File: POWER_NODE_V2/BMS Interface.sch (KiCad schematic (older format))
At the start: 11 parts, among them J10 CONN_02X07, J9 CONN_01X02, U12 NCV8405ADTRKG, U13 MAX14850AEE+, U14 MAX14850AEE+

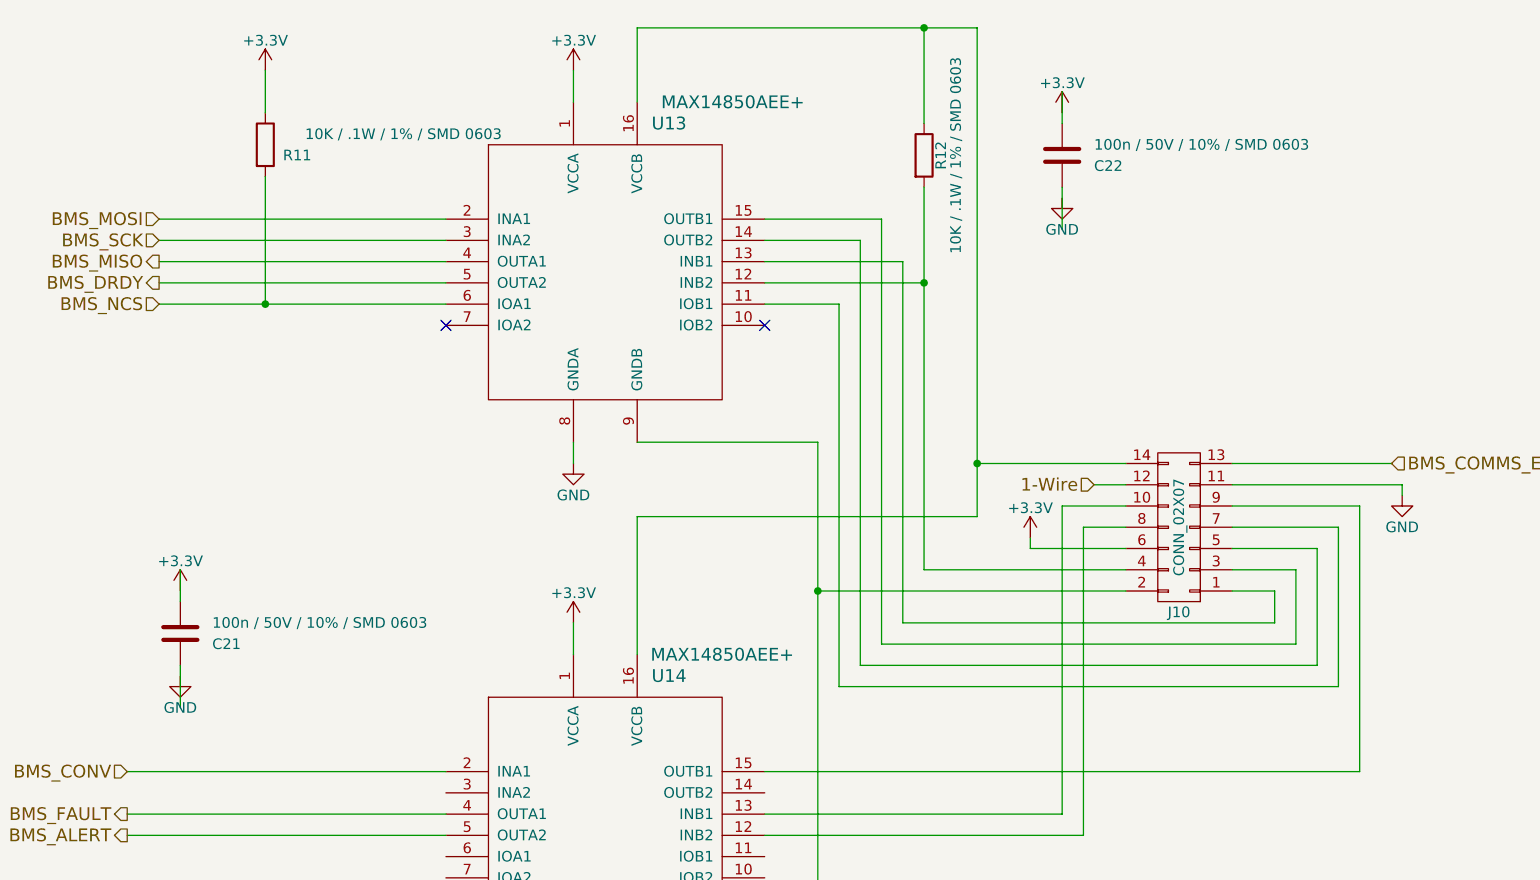
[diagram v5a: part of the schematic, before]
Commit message: Power Node v2 WIP
TODO: 3d models, double check everything, update connector P/N on
schematics, align boards and drill holes
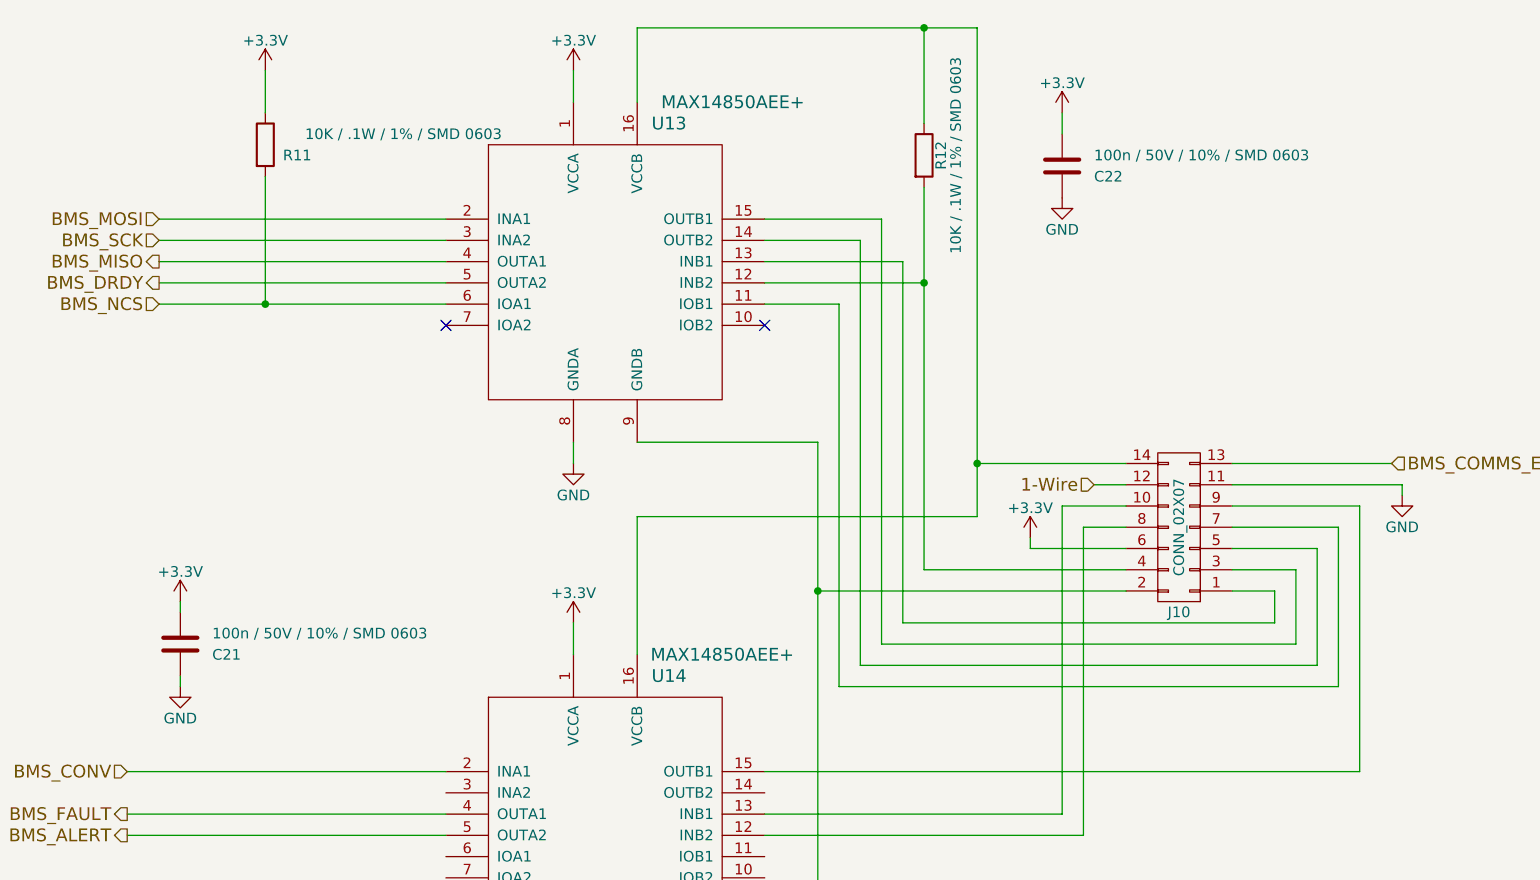
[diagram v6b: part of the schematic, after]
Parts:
- J9: footprint Pin_Headers:Pin_Header_Straight_1x02_Pitch2.54mm -> rLoop Footprints:TE_1744055-2_3.96_EP_HDR_ASSY_2P_VERT_HT
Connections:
- wire segments 78 -> 77
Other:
- moved on the sheet: C21, C22
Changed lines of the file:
@@
 F 0 "J9" H 5150 6700 50  0000 C CNN
 F 1 "CONN_01X02" V 5250 6550 50  0000 C CNN
-F 2 "Pin_Headers:Pin_Header_Straight_1x02_Pitch2.54mm" H 5150 6550 50  0001 C CNN
+F 2 "rLoop Footprints:TE_1744055-2_3.96_EP_HDR_ASSY_2P_VERT_HT" H 5150 6550 50  0001 C CNN
 F 3 "" H 5150 6550 50  0001 C CNN
 	1    5150 6550
@@
 L C C22
 U 1 1 59514BAA
-P 6450 1750
-F 0 "C22" H 6600 1700 50  0000 L CNN
-F 1 "100n / 50V / 10% / SMD 0603" H 6600 1800 50  0000 L CNN
-F 2 "Capacitors_SMD:C_0603" H 6488 1600 50  0001 C CNN
-F 3 "" H 6450 1750 50  0001 C CNN
-	1    6450 1750
+P 6450 1800
+F 0 "C22" H 6600 1750 50  0000 L CNN
+F 1 "100n / 50V / 10% / SMD 0603" H 6600 1850 50  0000 L CNN
+F 2 "Capacitors_SMD:C_0603" H 6488 1650 50  0001 C CNN
+F 3 "" H 6450 1800 50  0001 C CNN
+	1    6450 1800
 	1    0    0    -1
 $EndComp
@@
 $EndComp
 $Comp
-L GND #PWR0107
-U 1 1 59514D0B
-P 6450 1950
-F 0 "#PWR0107" H 6450 1700 50  0001 C CNN
-F 1 "GND" H 6450 1800 50  0000 C CNN
-F 2 "" H 6450 1950 50  0001 C CNN
-F 3 "" H 6450 1950 50  0001 C CNN
-	1    6450 1950
-	1    0    0    -1
-$EndComp
-$Comp
 L C C21
 U 1 1 59515426
-P 2300 4000
-F 0 "C21" H 2450 3950 50  0000 L CNN
-F 1 "100n / 50V / 10% / SMD 0603" H 2450 4050 50  0000 L CNN
-F 2 "Capacitors_SMD:C_0603" H 2338 3850 50  0001 C CNN
-F 3 "" H 2300 4000 50  0001 C CNN
-	1    2300 4000
-	1    0    0    -1
-$EndComp
-$Comp
-L +3.3V #PWR0108
+P 2300 4050
+F 0 "C21" H 2450 4000 50  0000 L CNN
+F 1 "100n / 50V / 10% / SMD 0603" H 2450 4100 50  0000 L CNN
+F 2 "Capacitors_SMD:C_0603" H 2338 3900 50  0001 C CNN
+F 3 "" H 2300 4050 50  0001 C CNN
+	1    2300 4050
+	1    0    0    -1
+$EndComp
+$Comp
+L +3.3V #PWR0107
 U 1 1 5951542C
-P 2300 3800
-F 0 "#PWR0108" H 2300 3650 50  0001 C CNN
-F 1 "+3.3V" H 2300 3940 50  0000 C CNN
-F 2 "" H 2300 3800 50  0001 C CNN
-F 3 "" H 2300 3800 50  0001 C CNN
-	1    2300 3800
-	1    0    0    -1
-$EndComp
-$Comp
-L GND #PWR0109
+P 2300 3850
+F 0 "#PWR0107" H 2300 3700 50  0001 C CNN
+F 1 "+3.3V" H 2300 3990 50  0000 C CNN
+F 2 "" H 2300 3850 50  0001 C CNN
+F 3 "" H 2300 3850 50  0001 C CNN
+	1    2300 3850
+	1    0    0    -1
+$EndComp
+$Comp
+L GND #PWR0108
 U 1 1 59515432
-P 2300 4200
-F 0 "#PWR0109" H 2300 3950 50  0001 C CNN
-F 1 "GND" H 2300 4050 50  0000 C CNN
-F 2 "" H 2300 4200 50  0001 C CNN
-F 3 "" H 2300 4200 50  0001 C CNN
-	1    2300 4200
+P 2300 4250
+F 0 "#PWR0108" H 2300 4000 50  0001 C CNN
+F 1 "GND" H 2300 4100 50  0000 C CNN
+F 2 "" H 2300 4250 50  0001 C CNN
+F 3 "" H 2300 4250 50  0001 C CNN
+	1    2300 4250
 	1    0    0    -1
 $EndComp
@@
 	0    1    1    0
 $EndComp
-Wire Wire Line
-	2200 2050 3550 2050
-Wire Wire Line
-	3550 2150 2200 2150
-Wire Wire Line
-	2200 2250 3550 2250
-Wire Wire Line
-	2200 2350 3550 2350
-Wire Wire Line
-	2050 4650 3550 4650
-Wire Wire Line
-	3550 4850 2050 4850
-Wire Wire Line
-	2050 4950 3550 4950
-Wire Wire Line
-	2200 2450 3550 2450
-Wire Wire Line
-	7250 3200 8000 3200
-Wire Wire Line
-	7250 3300 8050 3300
-Wire Wire Line
-	8050 3300 8050 3350
-Wire Wire Line
-	7250 3400 7850 3400
-Wire Wire Line
-	7850 3400 7850 4650
-Wire Wire Line
-	7850 4650 5050 4650
-Wire Wire Line
-	7250 3500 7750 3500
-Wire Wire Line
-	7750 3500 7750 4250
-Wire Wire Line
-	7750 4250 5400 4250
-Wire Wire Line
-	5400 4250 5400 2450
-Wire Wire Line
-	7250 3600 7650 3600
-Wire Wire Line
-	7650 3600 7650 4150
-Wire Wire Line
-	7650 4150 5500 4150
-Wire Wire Line
-	5500 4150 5500 2150
-Wire Wire Line
-	5500 2150 5050 2150
-Wire Wire Line
-	5400 2450 5050 2450
-Wire Wire Line
-	7250 3700 7550 3700
-Wire Wire Line
-	7550 3700 7550 4050
-Wire Wire Line
-	7550 4050 5600 4050
-Wire Wire Line
-	5600 4050 5600 2050
-Wire Wire Line
-	5600 2050 5050 2050
-Wire Wire Line
-	7250 3800 7450 3800
-Wire Wire Line
-	7450 3800 7450 3950
-Wire Wire Line
-	7450 3950 5700 3950
-Wire Wire Line
-	5700 3950 5700 2250
-Wire Wire Line
-	5700 2250 5050 2250
-Wire Wire Line
-	6750 3800 5300 3800
-Wire Wire Line
-	5300 3100 5300 5800
-Wire Wire Line
-	5300 3100 4450 3100
-Wire Wire Line
-	5300 5800 4450 5800
-Wire Wire Line
-	4450 5800 4450 5700
-Connection ~ 5300 3800
-Wire Wire Line
-	5800 3700 6750 3700
-Wire Wire Line
-	5800 1900 5800 3700
-Wire Wire Line
-	5800 2350 5050 2350
-Wire Wire Line
-	6300 3550 6300 3600
-Wire Wire Line
-	6300 3600 6750 3600
-Wire Wire Line
-	6750 3500 6550 3500
-Wire Wire Line
-	6550 3500 6550 4950
-Wire Wire Line
-	6550 4950 5050 4950
-Wire Wire Line
-	6750 3400 6450 3400
-Wire Wire Line
-	6450 3400 6450 4850
-Wire Wire Line
-	6450 4850 5050 4850
-Wire Wire Line
-	6750 3200 6050 3200
-Wire Wire Line
-	6050 1150 6050 3450
-Wire Wire Line
-	4450 1150 6050 1150
-Wire Wire Line
-	4450 1150 4450 1500
-Wire Wire Line
-	6050 3450 4450 3450
-Wire Wire Line
-	4450 3450 4450 4100
-Connection ~ 6050 3200
-Wire Wire Line
-	6600 3300 6750 3300
-Wire Wire Line
-	2700 1850 2700 2450
-Connection ~ 2700 2450
-Connection ~ 5800 2350
-Wire Wire Line
-	5800 1600 5800 1150
-Connection ~ 5800 1150
-Wire Wire Line
-	2700 1550 2700 1350
-Wire Wire Line
-	4150 1350 4150 1500
-Wire Wire Line
-	4150 3950 4150 4100
-Wire Wire Line
-	4150 3200 4150 3100
-Wire Wire Line
-	4150 5800 4150 5700
-Wire Wire Line
-	4700 6600 4700 7150
-Wire Wire Line
-	4950 6600 4700 6600
-Wire Wire Line
-	4700 6300 4700 6500
-Wire Wire Line
-	4700 6500 4950 6500
-Wire Wire Line
-	2350 7150 1800 7150
-Wire Wire Line
-	6450 2100 6450 1900
-Wire Wire Line
-	6450 1600 6450 1450
-Wire Wire Line
-	2300 4350 2300 4150
-Wire Wire Line
-	2300 3850 2300 3700
-Wire Wire Line
-	4400 6450 4700 6450
-Connection ~ 4700 6450
-Wire Wire Line
-	4400 6750 4700 6750
-Connection ~ 4700 6750
 $Comp
 L NCV8405ADTRKG U12
@@
 	1    0    0    -1
 $EndComp
-Wire Wire Line
-	2650 7150 3250 7150
-Wire Wire Line
-	4700 7150 4300 7150
-Wire Wire Line
-	3750 7700 3750 7550
 Text Notes 6400 7200 0    197  ~ 0
 BMS Interface
+$Comp
+L GND #PWR0109
+U 1 1 59514D0B
+P 6450 1950
+F 0 "#PWR0109" H 6450 1700 50  0001 C CNN
+F 1 "GND" H 6450 1800 50  0000 C CNN
+F 2 "" H 6450 1950 50  0001 C CNN
+F 3 "" H 6450 1950 50  0001 C CNN
+	1    6450 1950
+	1    0    0    -1
+$EndComp
+Wire Wire Line
+	2200 2050 3550 2050
+Wire Wire Line
+	3550 2150 2200 2150
+Wire Wire Line
+	2200 2250 3550 2250
+Wire Wire Line
+	2200 2350 3550 2350
+Wire Wire Line
+	2050 4650 3550 4650
+Wire Wire Line
+	3550 4850 2050 4850
+Wire Wire Line
+	2050 4950 3550 4950
+Wire Wire Line
+	2200 2450 3550 2450
+Wire Wire Line
+	7250 3200 8000 3200
+Wire Wire Line
+	7250 3300 8050 3300
+Wire Wire Line
+	8050 3300 8050 3350
+Wire Wire Line
+	7250 3400 7850 3400
+Wire Wire Line
+	7850 3400 7850 4650
+Wire Wire Line
+	7850 4650 5050 4650
+Wire Wire Line
+	7250 3500 7750 3500
+Wire Wire Line
+	7750 3500 7750 4250
+Wire Wire Line
+	7750 4250 5400 4250
+Wire Wire Line
+	5400 4250 5400 2450
+Wire Wire Line
+	7250 3600 7650 3600
+Wire Wire Line
+	7650 3600 7650 4150
+Wire Wire Line
+	7650 4150 5500 4150
+Wire Wire Line
+	5500 4150 5500 2150
+Wire Wire Line
+	5500 2150 5050 2150
+Wire Wire Line
+	5400 2450 5050 2450
+Wire Wire Line
+	7250 3700 7550 3700
+Wire Wire Line
+	7550 3700 7550 4050
+Wire Wire Line
+	7550 4050 5600 4050
+Wire Wire Line
+	5600 4050 5600 2050
+Wire Wire Line
+	5600 2050 5050 2050
+Wire Wire Line
+	7250 3800 7450 3800
+Wire Wire Line
+	7450 3800 7450 3950
+Wire Wire Line
+	7450 3950 5700 3950
+Wire Wire Line
+	5700 3950 5700 2250
+Wire Wire Line
+	5700 2250 5050 2250
+Wire Wire Line
+	6750 3800 5300 3800
+Wire Wire Line
+	5300 3100 5300 5800
+Wire Wire Line
+	5300 3100 4450 3100
+Wire Wire Line
+	5300 5800 4450 5800
+Wire Wire Line
+	4450 5800 4450 5700
+Connection ~ 5300 3800
+Wire Wire Line
+	5800 3700 6750 3700
+Wire Wire Line
+	5800 1900 5800 3700
+Wire Wire Line
+	5800 2350 5050 2350
+Wire Wire Line
+	6300 3550 6300 3600
+Wire Wire Line
+	6300 3600 6750 3600
+Wire Wire Line
+	6750 3500 6550 3500
+Wire Wire Line
+	6550 3500 6550 4950
+Wire Wire Line
+	6550 4950 5050 4950
+Wire Wire Line
+	6750 3400 6450 3400
+Wire Wire Line
+	6450 3400 6450 4850
+Wire Wire Line
+	6450 4850 5050 4850
+Wire Wire Line
+	6750 3200 6050 3200
+Wire Wire Line
+	6050 1150 6050 3450
+Wire Wire Line
+	4450 1150 6050 1150
+Wire Wire Line
+	4450 1150 4450 1500
+Wire Wire Line
+	6050 3450 4450 3450
+Wire Wire Line
+	4450 3450 4450 4100
+Connection ~ 6050 3200
+Wire Wire Line
+	6600 3300 6750 3300
+Wire Wire Line
+	2700 1850 2700 2450
+Connection ~ 2700 2450
+Connection ~ 5800 2350
+Wire Wire Line
+	5800 1600 5800 1150
+Connection ~ 5800 1150
+Wire Wire Line
+	2700 1550 2700 1350
+Wire Wire Line
+	4150 1350 4150 1500
+Wire Wire Line
+	4150 3950 4150 4100
+Wire Wire Line
+	4150 3200 4150 3100
+Wire Wire Line
+	4150 5800 4150 5700
+Wire Wire Line
+	4700 6600 4700 7150
+Wire Wire Line
+	4950 6600 4700 6600
+Wire Wire Line
+	4700 6300 4700 6500
+Wire Wire Line
+	4700 6500 4950 6500
+Wire Wire Line
+	2350 7150 1800 7150
+Wire Wire Line
+	2300 4250 2300 4200
+Wire Wire Line
+	2300 3900 2300 3850
+Wire Wire Line
+	4400 6450 4700 6450
+Connection ~ 4700 6450
+Wire Wire Line
+	4400 6750 4700 6750
+Connection ~ 4700 6750
+Wire Wire Line
+	2650 7150 3250 7150
+Wire Wire Line
+	4700 7150 4300 7150
+Wire Wire Line
+	3750 7700 3750 7550
+Wire Wire Line
+	6450 1550 6450 1650
 $EndSCHEMATC

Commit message: Lot's of progress
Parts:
- J9: value CONN_01X02 -> TE_3-641119-2; footprint rLoop Footprints:TE_1744055-2_3.96_EP_HDR_ASSY_2P_VERT_HT -> rLoop_Footprints:3-641119-2_TE_2P_MTA156_HDR
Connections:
- net +24V: now also J9.2 (P2); no longer J9.1 (P1)
- net at D6.2 (A), U12.4 (Drain): now also J9.1 (P1); no longer J9.2 (P2)
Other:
- moved on the sheet: D6, J9
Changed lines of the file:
@@
 L CONN_01X02 J9
 U 1 1 594DEEA6
-P 5150 6550
-F 0 "J9" H 5150 6700 50  0000 C CNN
-F 1 "CONN_01X02" V 5250 6550 50  0000 C CNN
-F 2 "rLoop Footprints:TE_1744055-2_3.96_EP_HDR_ASSY_2P_VERT_HT" H 5150 6550 50  0001 C CNN
-F 3 "" H 5150 6550 50  0001 C CNN
-	1    5150 6550
-	1    0    0    -1
+P 4400 6550
+F 0 "J9" H 4400 6700 50  0000 C CNN
+F 1 "TE_3-641119-2" V 4500 6550 50  0000 C CNN
+F 2 "rLoop_Footprints:3-641119-2_TE_2P_MTA156_HDR" H 4400 6550 50  0001 C CNN
+F 3 "" H 4400 6550 50  0001 C CNN
+	1    4400 6550
+	-1   0    0    1
 $EndComp
 $Comp
@@
 L D D6
 U 1 1 595161C1
-P 4400 6600
-F 0 "D6" V 4450 6350 50  0000 C CNN
-F 1 "IN4004" V 4350 6400 50  0000 C CNN
-F 2 "Diodes_THT:D_DO-201_P15.24mm_Horizontal" H 4400 6600 50  0001 C CNN
-F 3 "" H 4400 6600 50  0001 C CNN
-	1    4400 6600
+P 5200 6600
+F 0 "D6" V 5250 6350 50  0000 C CNN
+F 1 "IN4004" V 5150 6400 50  0000 C CNN
+F 2 "Diodes_THT:D_DO-201_P15.24mm_Horizontal" H 5200 6600 50  0001 C CNN
+F 3 "" H 5200 6600 50  0001 C CNN
+	1    5200 6600
 	0    1    1    0
 $EndComp
@@
 	4700 6600 4700 7150
 Wire Wire Line
-	4950 6600 4700 6600
-Wire Wire Line
 	4700 6300 4700 6500
 Wire Wire Line
-	4700 6500 4950 6500
-Wire Wire Line
 	2350 7150 1800 7150
 Wire Wire Line
@@
 	2300 3900 2300 3850
 Wire Wire Line
-	4400 6450 4700 6450
+	5200 6450 4700 6450
 Connection ~ 4700 6450
 Wire Wire Line
-	4400 6750 4700 6750
+	5200 6750 4700 6750
 Connection ~ 4700 6750
 Wire Wire Line
@@
 Wire Wire Line
 	6450 1550 6450 1650
+Wire Wire Line
+	4700 6500 4600 6500
+Wire Wire Line
+	4700 6600 4600 6600
 $EndSCHEMATC

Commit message: All modelled, schematics and mechanical just need a double check
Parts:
- J10: value CONN_02X07 -> 5-534998-7
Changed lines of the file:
@@
 P 7000 3500
 F 0 "J10" H 7000 3900 50  0000 C CNN
-F 1 "CONN_02X07" V 7000 3500 50  0000 C CNN
+F 1 "5-534998-7" V 7000 3500 50  0000 C CNN
 F 2 "Pin_Headers:Pin_Header_Straight_2x07_Pitch2.54mm" H 7000 2300 50  0001 C CNN
 F 3 "" H 7000 2300 50  0001 C CNN
@@
 $EndComp
 $Comp
-L GND #PWR097
+L GND #PWR096
 U 1 1 594CA92D
 P 8050 3350
-F 0 "#PWR097" H 8050 3100 50  0001 C CNN
+F 0 "#PWR096" H 8050 3100 50  0001 C CNN
 F 1 "GND" H 8050 3200 50  0000 C CNN
 F 2 "" H 8050 3350 50  0001 C CNN
@@
 $EndComp
 $Comp
-L +3.3V #PWR098
+L +3.3V #PWR097
 U 1 1 594CAB5E
 P 6300 3550
-F 0 "#PWR098" H 6300 3400 50  0001 C CNN
+F 0 "#PWR097" H 6300 3400 50  0001 C CNN
 F 1 "+3.3V" H 6300 3690 50  0000 C CNN
 F 2 "" H 6300 3550 50  0001 C CNN
@@
 $EndComp
 $Comp
-L +3.3V #PWR099
+L +3.3V #PWR098
 U 1 1 594CBADD
 P 4150 1350
-F 0 "#PWR099" H 4150 1200 50  0001 C CNN
+F 0 "#PWR098" H 4150 1200 50  0001 C CNN
 F 1 "+3.3V" H 4150 1490 50  0000 C CNN
 F 2 "" H 4150 1350 50  0001 C CNN
@@
 $EndComp
 $Comp
-L +3.3V #PWR0100
+L +3.3V #PWR099
 U 1 1 594CBAF4
 P 2700 1350
-F 0 "#PWR0100" H 2700 1200 50  0001 C CNN
+F 0 "#PWR099" H 2700 1200 50  0001 C CNN
 F 1 "+3.3V" H 2700 1490 50  0000 C CNN
 F 2 "" H 2700 1350 50  0001 C CNN
@@
 $EndComp
 $Comp
-L +3.3V #PWR0101
+L +3.3V #PWR0100
 U 1 1 594CBB5B
 P 4150 3950
-F 0 "#PWR0101" H 4150 3800 50  0001 C CNN
+F 0 "#PWR0100" H 4150 3800 50  0001 C CNN
 F 1 "+3.3V" H 4150 4090 50  0000 C CNN
 F 2 "" H 4150 3950 50  0001 C CNN
@@
 $EndComp
 $Comp
-L GND #PWR0102
+L GND #PWR0101
 U 1 1 594CBF3C
 P 4150 3200
-F 0 "#PWR0102" H 4150 2950 50  0001 C CNN
+F 0 "#PWR0101" H 4150 2950 50  0001 C CNN
 F 1 "GND" H 4150 3050 50  0000 C CNN
 F 2 "" H 4150 3200 50  0001 C CNN
@@
 $EndComp
 $Comp
-L GND #PWR0103
+L GND #PWR0102
 U 1 1 594CBFA2
 P 4150 5800
-F 0 "#PWR0103" H 4150 5550 50  0001 C CNN
+F 0 "#PWR0102" H 4150 5550 50  0001 C CNN
 F 1 "GND" H 4150 5650 50  0000 C CNN
 F 2 "" H 4150 5800 50  0001 C CNN
@@
 $EndComp
 $Comp
-L GND #PWR0104
+L GND #PWR0103
 U 1 1 594DF3E0
 P 3750 7700
-F 0 "#PWR0104" H 3750 7450 50  0001 C CNN
+F 0 "#PWR0103" H 3750 7450 50  0001 C CNN
 F 1 "GND" H 3750 7550 50  0000 C CNN
 F 2 "" H 3750 7700 50  0001 C CNN
@@
 $EndComp
 $Comp
-L +24V #PWR0105
+L +24V #PWR0104
 U 1 1 594DF525
 P 4700 6300
-F 0 "#PWR0105" H 4700 6150 50  0001 C CNN
+F 0 "#PWR0104" H 4700 6150 50  0001 C CNN
 F 1 "+24V" H 4700 6440 50  0000 C CNN
 F 2 "" H 4700 6300 50  0001 C CNN
@@
 $EndComp
 $Comp
-L +3.3V #PWR0106
+L +3.3V #PWR0105
 U 1 1 59514C06
 P 6450 1550
-F 0 "#PWR0106" H 6450 1400 50  0001 C CNN
+F 0 "#PWR0105" H 6450 1400 50  0001 C CNN
 F 1 "+3.3V" H 6450 1690 50  0000 C CNN
 F 2 "" H 6450 1550 50  0001 C CNN
@@
 $EndComp
 $Comp
-L +3.3V #PWR0107
+L +3.3V #PWR0106
 U 1 1 5951542C
 P 2300 3850
-F 0 "#PWR0107" H 2300 3700 50  0001 C CNN
+F 0 "#PWR0106" H 2300 3700 50  0001 C CNN
 F 1 "+3.3V" H 2300 3990 50  0000 C CNN
 F 2 "" H 2300 3850 50  0001 C CNN
@@
 $EndComp
 $Comp
-L GND #PWR0108
+L GND #PWR0107
 U 1 1 59515432
 P 2300 4250
-F 0 "#PWR0108" H 2300 4000 50  0001 C CNN
+F 0 "#PWR0107" H 2300 4000 50  0001 C CNN
 F 1 "GND" H 2300 4100 50  0000 C CNN
 F 2 "" H 2300 4250 50  0001 C CNN
@@
 BMS Interface
 $Comp
-L GND #PWR0109
+L GND #PWR0108
 U 1 1 59514D0B
 P 6450 1950
-F 0 "#PWR0109" H 6450 1700 50  0001 C CNN
+F 0 "#PWR0108" H 6450 1700 50  0001 C CNN
 F 1 "GND" H 6450 1800 50  0000 C CNN
 F 2 "" H 6450 1950 50  0001 C CNN
